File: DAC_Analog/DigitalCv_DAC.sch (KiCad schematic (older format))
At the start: 78 parts, among them J10 Fix, J11 Fix, J12 Fix, J13 Fix, J14 MCLK_Test, T1 DA103C, T2 DA103C, T3 DA103C, T4 DA103C, U12 TPS79318, U13 SRC4392, U14 TPS79333, U15 TPS79333, U16 REG104_DCQ, U17 PCM1792A, U18 DS90LV012ATMF, U19 LMK61E2

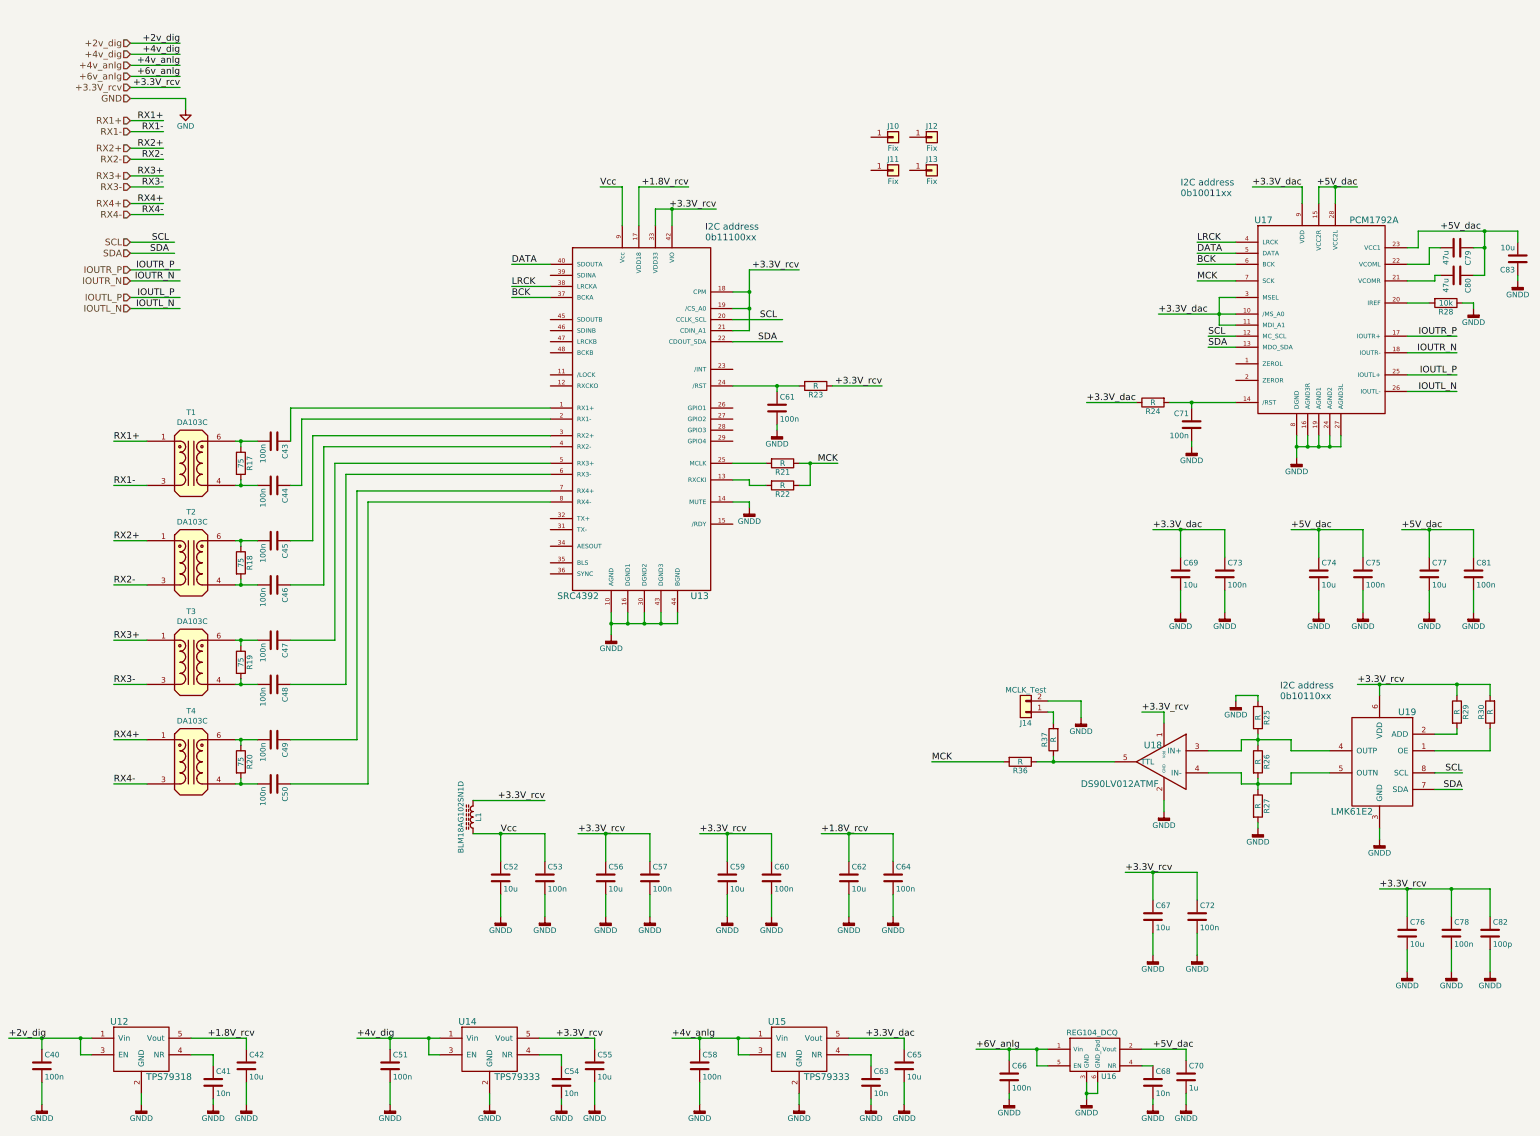
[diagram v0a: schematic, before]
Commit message: Send Gerber DAC_Analog and DAC_Digital
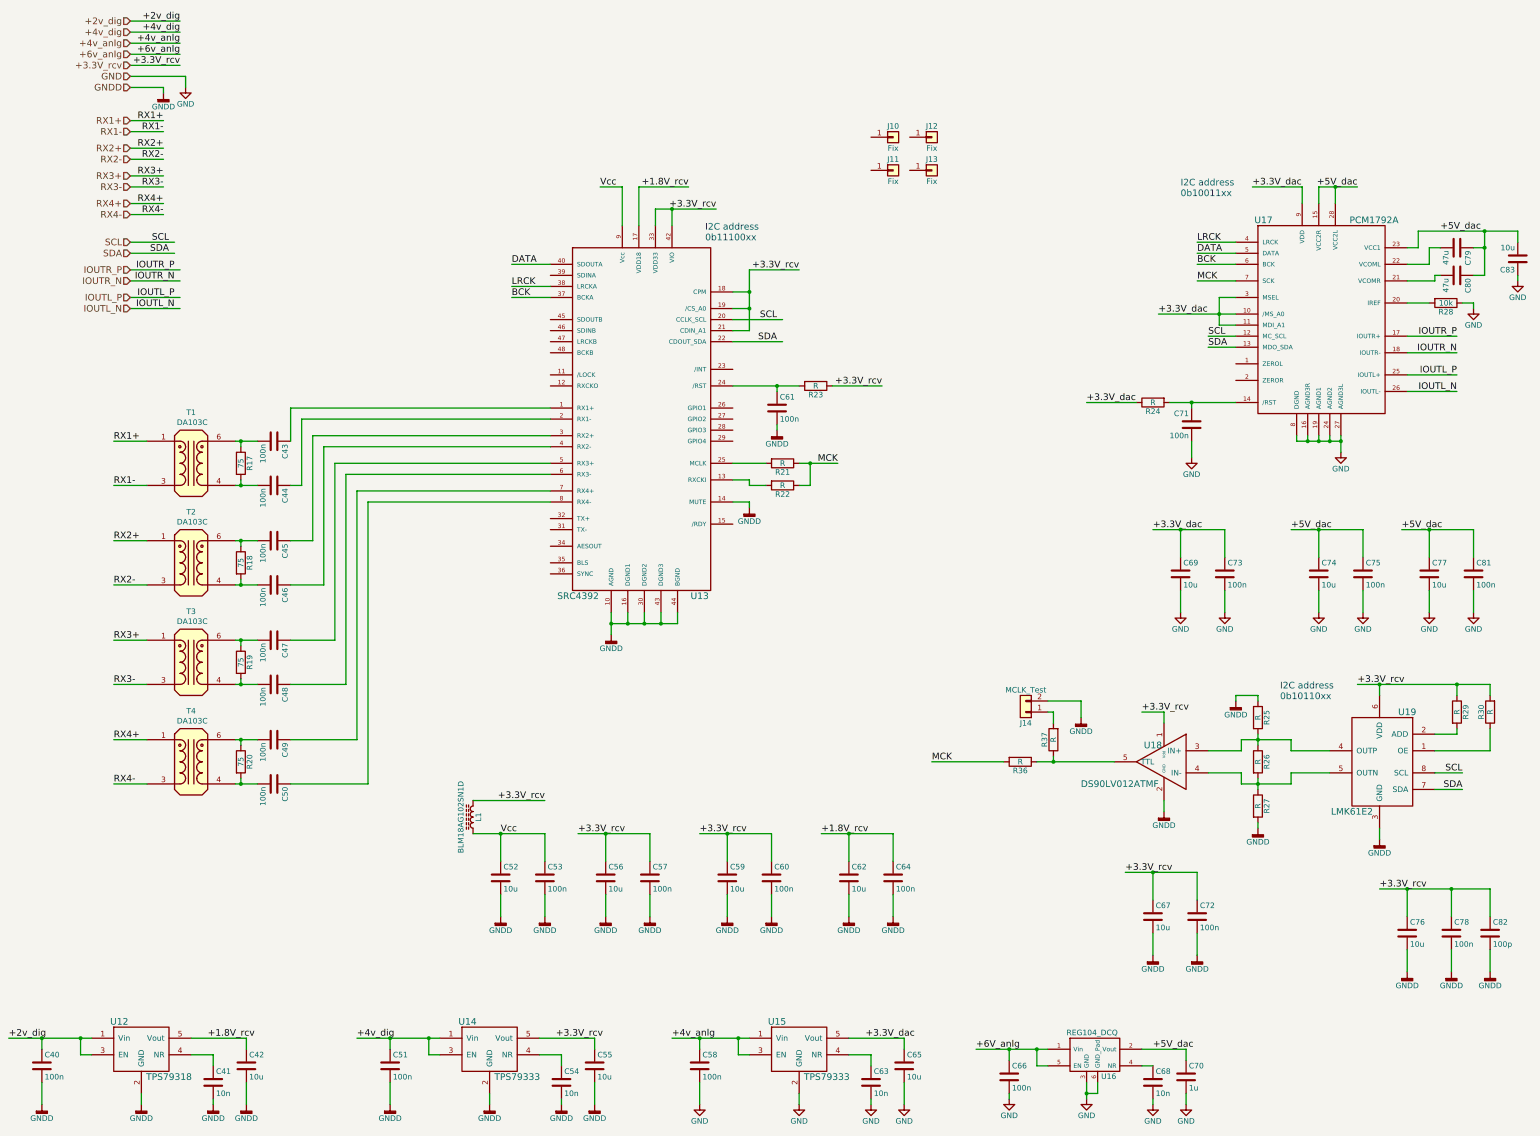
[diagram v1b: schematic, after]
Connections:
- net GND: now also C58.2, C63.2, C65.2, C66.2, C68.2, C69.2, C70.2, C71.2, C73.2, C74.2, C75.2, C77.2, C81.2, C83.1, R28.1, U15.2 (GND), U16.3 (GND), U16.6 (GND_Pad), U17.16 (AGND3R), U17.19 (AGND1), U17.24 (AGND2), U17.27 (AGND3L), U17.8 (DGND)
- net GNDD: no longer C58.2, C63.2, C65.2, C66.2, C68.2, C69.2, C70.2, C71.2, C73.2, C74.2, C75.2, C77.2, C81.2, C83.1, R28.1, U15.2 (GND), U16.3 (GND), U16.6 (GND_Pad), U17.16 (AGND3R), U17.19 (AGND1), U17.24 (AGND2), U17.27 (AGND3L), U17.8 (DGND)

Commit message: Update gnd connection on digital transformer
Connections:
- net GNDD: now also C44.2, C46.2, C48.2, C50.2, R17.2, R18.2, R19.2, R20.2, T1.4 (SA), T2.4 (SA), T3.4 (SA), T4.4 (SA)
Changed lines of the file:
@@
 	2700 5000 2900 5000
 Wire Wire Line
-	2750 4950 2750 5000
+	2750 4950 2750 5050
 Connection ~ 2750 5000
 Wire Wire Line
@@
 	2700 5900 2900 5900
 Wire Wire Line
-	2750 5850 2750 5900
+	2750 5850 2750 5950
 Connection ~ 2750 5900
 Wire Wire Line
@@
 	2700 6800 2900 6800
 Wire Wire Line
-	2750 6750 2750 6800
+	2750 6750 2750 6850
 Connection ~ 2750 6800
 Wire Wire Line
@@
 	2700 7700 2900 7700
 Wire Wire Line
-	2750 7650 2750 7700
+	2750 7650 2750 7750
 Connection ~ 2750 7700
 Wire Wire Line
@@
 $EndComp
 Wire Wire Line
-	10650 7500 9950 7500
+	9950 7500 10650 7500
 Wire Wire Line
 	10100 7450 10100 7500
@@
 	-1   0    0    -1
 $EndComp
+$Comp
+L GNDD #PWR?
+U 1 1 5AB6FC53
+P 2750 7750
+F 0 "#PWR?" H 2750 7500 50  0001 C CNN
+F 1 "GNDD" H 2750 7625 50  0000 C CNN
+F 2 "" H 2750 7750 50  0001 C CNN
+F 3 "" H 2750 7750 50  0001 C CNN
+	1    2750 7750
+	1    0    0    -1
+$EndComp
+$Comp
+L GNDD #PWR?
+U 1 1 5AB6FCA7
+P 2750 5050
+F 0 "#PWR?" H 2750 4800 50  0001 C CNN
+F 1 "GNDD" H 2750 4925 50  0000 C CNN
+F 2 "" H 2750 5050 50  0001 C CNN
+F 3 "" H 2750 5050 50  0001 C CNN
+	1    2750 5050
+	1    0    0    -1
+$EndComp
+$Comp
+L GNDD #PWR?
+U 1 1 5AB6FCFB
+P 2750 5950
+F 0 "#PWR?" H 2750 5700 50  0001 C CNN
+F 1 "GNDD" H 2750 5825 50  0000 C CNN
+F 2 "" H 2750 5950 50  0001 C CNN
+F 3 "" H 2750 5950 50  0001 C CNN
+	1    2750 5950
+	1    0    0    -1
+$EndComp
+$Comp
+L GNDD #PWR?
+U 1 1 5AB6FD4F
+P 2750 6850
+F 0 "#PWR?" H 2750 6600 50  0001 C CNN
+F 1 "GNDD" H 2750 6725 50  0000 C CNN
+F 2 "" H 2750 6850 50  0001 C CNN
+F 3 "" H 2750 6850 50  0001 C CNN
+	1    2750 6850
+	1    0    0    -1
+$EndComp
 $EndSCHEMATC
